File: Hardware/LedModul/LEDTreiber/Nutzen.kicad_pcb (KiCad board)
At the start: 2 copper layers, 84 x 84 mm, 400 parts, among them J1 Conn_01x01_Pin, J2 Conn_01x01_Pin, J3 Conn_01x01_Pin, J4 Conn_01x01_Pin, J5 Conn_01x01_Pin, U1 TPS92200DxRXL, U2 TVS2700DRV

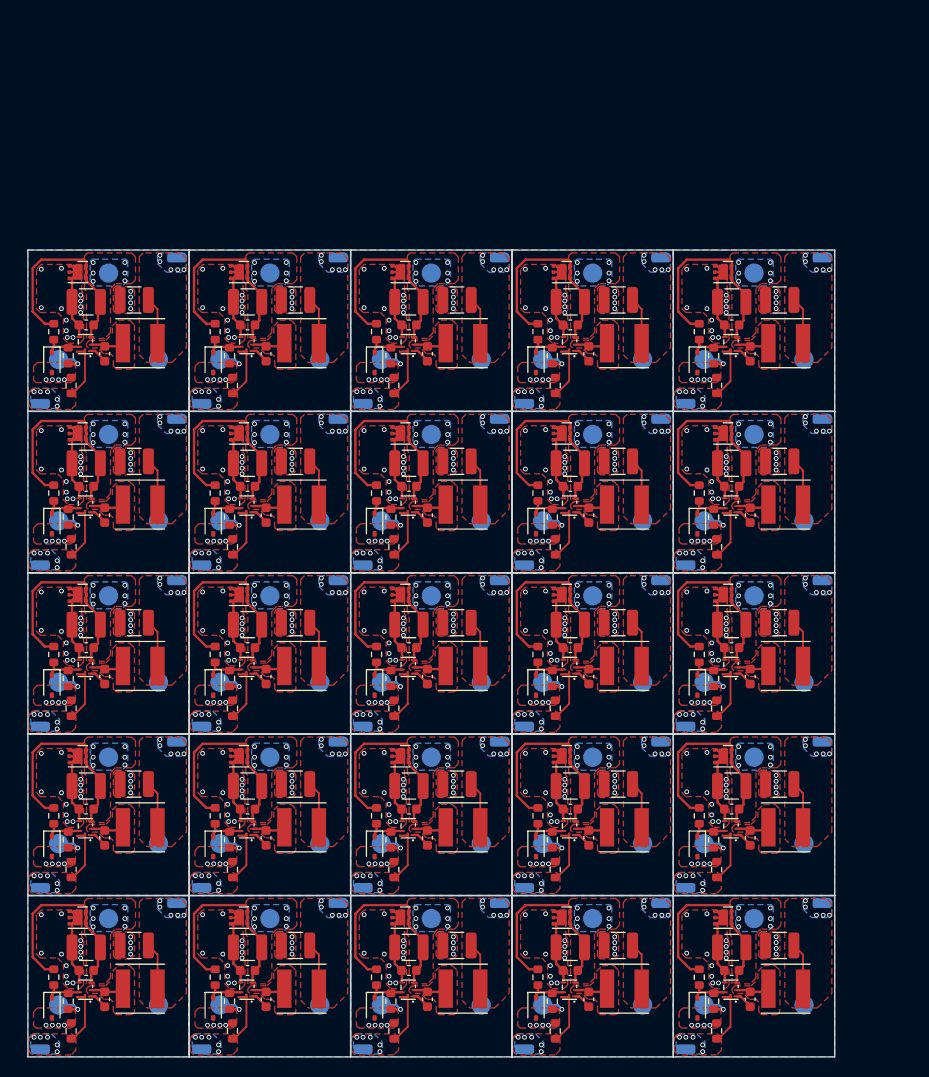
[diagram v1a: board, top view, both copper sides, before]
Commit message: added Pcb name and version to silkscreen
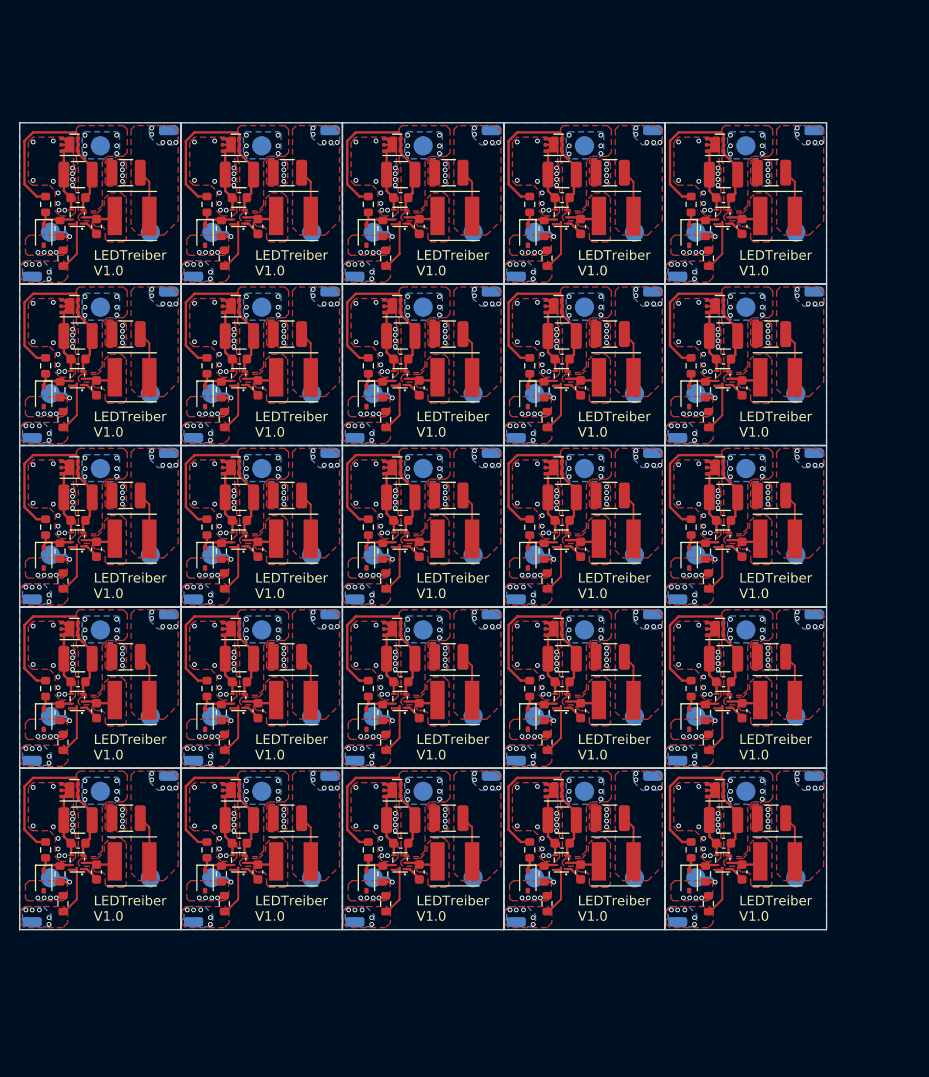
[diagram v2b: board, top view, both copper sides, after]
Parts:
- removed the C1 at (131.5, 94.8)
- removed the C1 at (131.5, 128.4)
- removed the C1 at (81.1, 94.8)
- removed the C1 at (97.9, 61.2)
- removed the C1 at (97.9, 128.4)
- removed the C1 at (81.1, 128.4)
- removed the C1 at (148.3, 94.8)
- removed the C1 at (131.5, 78.0)
- removed the C1 at (81.1, 61.2)
- removed the C1 at (114.7, 111.6)
- removed the C1 at (97.9, 78.0)
- removed the C1 at (114.7, 78.0)
- removed the C1 at (81.1, 78.0)
- removed the C1 at (131.5, 61.2)
- removed the C1 at (97.9, 111.6)
- removed the C1 at (114.7, 61.2)
- removed the C1 at (114.7, 94.8)
- removed the C1 at (97.9, 94.8)
- removed the C1 at (148.3, 111.6)
- removed the C1 at (148.3, 61.2)
- removed the C1 at (81.1, 111.6)
- removed the C1 at (148.3, 78.0)
- removed the C1 at (148.3, 128.4)
- removed the C1 at (131.5, 111.6)
- removed the C1 at (114.7, 128.4)
- removed the C2 at (128.4, 134.0)
- removed the C2 at (128.4, 66.8)
- removed the C2 at (111.6, 117.2)
- removed the C2 at (111.6, 66.8)
- removed the C2 at (128.4, 83.6)
- removed the C2 at (94.8, 100.4)
- removed the C2 at (94.8, 66.8)
- removed the C2 at (78.0, 134.0)
- removed the C2 at (145.2, 83.6)
- removed the C2 at (145.2, 66.8)
- removed the C2 at (94.8, 117.2)
- removed the C2 at (78.0, 117.2)
- removed the C2 at (78.0, 83.6)
- removed the C2 at (145.2, 134.0)
- removed the C2 at (128.4, 117.2)
- removed the C2 at (111.6, 100.4)
- removed the C2 at (111.6, 83.6)
- removed the C2 at (78.0, 100.4)
- removed the C2 at (111.6, 134.0)
- removed the C2 at (78.0, 66.8)
- removed the C2 at (94.8, 83.6)
- removed the C2 at (145.2, 100.4)
- removed the C2 at (94.8, 134.0)
- removed the C2 at (145.2, 117.2)
- removed the C2 at (128.4, 100.4)
- removed the C3 at (143.3, 111.8)
- removed the C3 at (143.3, 95.0)
- removed the C3 at (92.9, 128.6)
- removed the C3 at (92.9, 78.2)
- removed the C3 at (92.9, 95.0)
- removed the C3 at (126.5, 61.4)
- removed the C3 at (109.7, 61.4)
- removed the C3 at (143.3, 128.6)
- removed the C3 at (76.1, 95.0)
- removed the C3 at (126.5, 78.2)
- removed the C3 at (143.3, 61.4)
- removed the C3 at (109.7, 78.2)
- removed the C3 at (76.1, 78.2)
- removed the C3 at (109.7, 128.6)
- removed the C3 at (126.5, 128.6)
- removed the C3 at (76.1, 111.8)
- removed the C3 at (109.7, 95.0)
- removed the C3 at (109.7, 111.8)
- removed the C3 at (143.3, 78.2)
- removed the C3 at (126.5, 111.8)
- removed the C3 at (126.5, 95.0)
- removed the C3 at (76.1, 61.4)
- removed the C3 at (92.9, 61.4)
- removed the C3 at (76.1, 128.6)
- removed the C3 at (92.9, 111.8)
- removed the C4 at (143.3, 97.4)
- removed the C4 at (109.7, 63.8)
- removed the C4 at (143.3, 131.0)
- removed the C4 at (126.5, 97.4)
- removed the C4 at (76.1, 97.4)
- removed the C4 at (76.1, 63.8)
- removed the C4 at (109.7, 97.4)
- removed the C4 at (92.9, 63.8)
- removed the C4 at (143.3, 114.2)
- removed the C4 at (143.3, 80.6)
- removed the C4 at (109.7, 114.2)
- removed the C4 at (76.1, 80.6)
- removed the C4 at (109.7, 131.0)
- removed the C4 at (92.9, 131.0)
- removed the C4 at (143.3, 63.8)
- removed the C4 at (76.1, 114.2)
- removed the C4 at (92.9, 114.2)
- removed the C4 at (126.5, 114.2)
- removed the C4 at (109.7, 80.6)
- removed the C4 at (92.9, 80.6)
- removed the C4 at (76.1, 131.0)
- removed the C4 at (92.9, 97.4)
- removed the C4 at (126.5, 131.0)
- removed the C4 at (126.5, 80.6)
- removed the C4 at (126.5, 63.8)
- removed the D1 at (122.9, 84.5)
- removed the D1 at (89.3, 84.5)
- removed the D1 at (122.9, 134.9)
- removed the D1 at (139.7, 134.9)
- removed the D1 at (89.3, 134.9)
- removed the D1 at (89.3, 67.7)
- removed the D1 at (89.3, 101.3)
- removed the D1 at (106.1, 118.1)
- removed the D1 at (106.1, 101.3)
- removed the D1 at (72.5, 134.9)
- removed the D1 at (72.5, 84.5)
- removed the D1 at (89.3, 118.1)
- removed the D1 at (139.7, 118.1)
- removed the D1 at (139.7, 101.3)
- removed the D1 at (106.1, 67.7)
- removed the D1 at (139.7, 84.5)
- removed the D1 at (122.9, 101.3)
- removed the D1 at (72.5, 101.3)
- removed the D1 at (72.5, 67.7)
- removed the D1 at (122.9, 118.1)
- removed the D1 at (72.5, 118.1)
- removed the D1 at (122.9, 67.7)
- removed the D1 at (106.1, 134.9)
- removed the D1 at (106.1, 84.5)
- removed the D1 at (139.7, 67.7)
- removed the J1 at (135.9, 73.6)
- removed the J1 at (119.1, 124.0)
- removed the J1 at (152.7, 56.8)
- removed the J1 at (152.7, 124.0)
- removed the J1 at (102.3, 90.4)
- removed the J1 at (102.3, 73.6)
- removed the J1 at (85.5, 90.4)
- removed the J1 at (152.7, 73.6)
- removed the J1 at (135.9, 56.8)
- removed the J1 at (119.1, 90.4)
- removed the J1 at (135.9, 107.2)
- removed the J1 at (119.1, 56.8)
- removed the J1 at (152.7, 107.2)
- removed the J1 at (152.7, 90.4)
- removed the J1 at (85.5, 73.6)
- removed the J1 at (135.9, 124.0)
- removed the J1 at (85.5, 124.0)
- removed the J1 at (102.3, 56.8)
- removed the J1 at (102.3, 124.0)
- removed the J1 at (119.1, 73.6)
- removed the J1 at (119.1, 107.2)
- removed the J1 at (102.3, 107.2)
- removed the J1 at (85.5, 56.8)
- removed the J1 at (135.9, 90.4)
- removed the J1 at (85.5, 107.2)
- removed the J2 at (71.3, 122.4)
- removed the J2 at (71.3, 139.2)
- removed the J2 at (121.7, 105.6)
- removed the J2 at (104.9, 88.8)
- removed the J2 at (138.5, 88.8)
- removed the J2 at (104.9, 72.0)
- removed the J2 at (104.9, 139.2)
- removed the J2 at (138.5, 139.2)
- removed the J2 at (88.1, 88.8)
- removed the J2 at (71.3, 72.0)
- removed the J2 at (88.1, 122.4)
- removed the J2 at (104.9, 122.4)
- removed the J2 at (121.7, 88.8)
- removed the J2 at (88.1, 72.0)
- removed the J2 at (138.5, 122.4)
- removed the J2 at (138.5, 72.0)
- removed the J2 at (121.7, 122.4)
- removed the J2 at (121.7, 139.2)
- removed the J2 at (71.3, 88.8)
- removed the J2 at (121.7, 72.0)
- removed the J2 at (88.1, 139.2)
- removed the J2 at (104.9, 105.6)
- removed the J2 at (71.3, 105.6)
- removed the J2 at (88.1, 105.6)
- removed the J2 at (138.5, 105.6)
- removed the J3 at (123.6, 101.0)
- removed the J3 at (73.2, 84.2)
- removed the J3 at (73.2, 134.6)
- removed the J3 at (73.2, 67.4)
- removed the J3 at (106.8, 67.4)
- removed the J3 at (90.0, 101.0)
- removed the J3 at (123.6, 134.6)
- removed the J3 at (140.4, 101.0)
- removed the J3 at (140.4, 84.2)
- removed the J3 at (106.8, 84.2)
- removed the J3 at (123.6, 117.8)
- removed the J3 at (123.6, 67.4)
- removed the J3 at (106.8, 134.6)
- removed the J3 at (73.2, 117.8)
- removed the J3 at (90.0, 84.2)
- removed the J3 at (106.8, 101.0)
- removed the J3 at (106.8, 117.8)
- removed the J3 at (123.6, 84.2)
- removed the J3 at (90.0, 134.6)
- removed the J3 at (140.4, 67.4)
- removed the J3 at (90.0, 67.4)
- removed the J3 at (73.2, 101.0)
- removed the J3 at (90.0, 117.8)
- removed the J3 at (140.4, 117.8)
- removed the J3 at (140.4, 134.6)
- removed the J4 at (78.4, 75.2)
- removed the J4 at (145.6, 92.0)
- removed the J4 at (112.0, 92.0)
- removed the J4 at (78.4, 92.0)
- removed the J4 at (112.0, 108.8)
- removed the J4 at (128.8, 108.8)
- removed the J4 at (95.2, 92.0)
- removed the J4 at (145.6, 75.2)
- removed the J4 at (145.6, 58.4)
- removed the J4 at (95.2, 75.2)
- removed the J4 at (112.0, 75.2)
- removed the J4 at (78.4, 58.4)
- removed the J4 at (78.4, 125.6)
- removed the J4 at (128.8, 92.0)
- removed the J4 at (128.8, 125.6)
- removed the J4 at (95.2, 125.6)
- removed the J4 at (112.0, 58.4)
- removed the J4 at (78.4, 108.8)
- removed the J4 at (145.6, 108.8)
- removed the J4 at (95.2, 108.8)
- removed the J4 at (128.8, 58.4)
- removed the J4 at (145.6, 125.6)
- removed the J4 at (95.2, 58.4)
- removed the J4 at (112.0, 125.6)
- removed the J4 at (128.8, 75.2)
- removed the J5 at (83.6, 117.8)
- removed the J5 at (117.2, 134.6)
- removed the J5 at (134.0, 67.4)
- removed the J5 at (150.8, 117.8)
- removed the J5 at (100.4, 101.0)
- removed the J5 at (150.8, 134.6)
- removed the J5 at (100.4, 117.8)
- removed the J5 at (134.0, 117.8)
- removed the J5 at (117.2, 117.8)
- removed the J5 at (83.6, 101.0)
- removed the J5 at (150.8, 84.2)
- removed the J5 at (83.6, 67.4)
- removed the J5 at (134.0, 84.2)
- removed the J5 at (150.8, 67.4)
- removed the J5 at (83.6, 134.6)
- removed the J5 at (100.4, 134.6)
- removed the J5 at (100.4, 84.2)
- removed the J5 at (117.2, 84.2)
- removed the J5 at (83.6, 84.2)
- removed the J5 at (150.8, 101.0)
- removed the J5 at (117.2, 101.0)
- removed the J5 at (100.4, 67.4)
- removed the J5 at (117.2, 67.4)
- removed the J5 at (134.0, 134.6)
- removed the J5 at (134.0, 101.0)
- removed the L1 at (148.9, 82.5)
- removed the L1 at (98.5, 82.5)
- removed the L1 at (148.9, 99.3)
- removed the L1 at (115.3, 132.9)
- removed the L1 at (98.5, 116.1)
- removed the L1 at (81.7, 65.7)
- removed the L1 at (115.3, 82.5)
- removed the L1 at (81.7, 99.3)
- removed the L1 at (98.5, 65.7)
- removed the L1 at (81.7, 82.5)
- removed the L1 at (81.7, 132.9)
- removed the L1 at (115.3, 99.3)
- removed the L1 at (148.9, 65.7)
- removed the L1 at (98.5, 132.9)
- removed the L1 at (132.1, 132.9)
- removed the L1 at (98.5, 99.3)
- removed the L1 at (81.7, 116.1)
- removed the L1 at (148.9, 132.9)
- removed the L1 at (132.1, 65.7)
- removed the L1 at (115.3, 65.7)
- removed the L1 at (115.3, 116.1)
- removed the L1 at (132.1, 116.1)
- removed the L1 at (132.1, 99.3)
- removed the L1 at (148.9, 116.1)
- removed the L1 at (132.1, 82.5)
- removed the R1 at (123.1, 64.5)
- removed the R1 at (89.5, 64.5)
- removed the R1 at (123.1, 131.7)
- removed the R1 at (139.9, 98.1)
- removed the R1 at (89.5, 114.9)
- removed the R1 at (72.7, 81.3)
- removed the R1 at (106.3, 114.9)
- removed the R1 at (123.1, 98.1)
- removed the R1 at (106.3, 98.1)
- removed the R1 at (72.7, 131.7)
- removed the R1 at (139.9, 64.5)
- removed the R1 at (72.7, 64.5)
- removed the R1 at (123.1, 114.9)
- removed the R1 at (72.7, 114.9)
- removed the R1 at (89.5, 98.1)
- removed the R1 at (139.9, 81.3)
- removed the R1 at (139.9, 114.9)
- removed the R1 at (72.7, 98.1)
- removed the R1 at (106.3, 64.5)
- removed the R1 at (139.9, 131.7)
- removed the R1 at (106.3, 131.7)
- removed the R1 at (123.1, 81.3)
- removed the R1 at (89.5, 131.7)
- removed the R1 at (89.5, 81.3)
- removed the R1 at (106.3, 81.3)
- removed the R2 at (91.3, 86.9)
- removed the R2 at (141.7, 137.3)
- removed the R2 at (108.1, 103.7)
- removed the R2 at (91.3, 120.5)
- removed the R2 at (74.5, 120.5)
- removed the R2 at (91.3, 137.3)
- removed the R2 at (74.5, 137.3)
- removed the R2 at (124.9, 86.9)
- removed the R2 at (124.9, 137.3)
- removed the R2 at (108.1, 86.9)
- removed the R2 at (141.7, 103.7)
- removed the R2 at (108.1, 120.5)
- removed the R2 at (124.9, 120.5)
- removed the R2 at (124.9, 70.1)
- removed the R2 at (141.7, 70.1)
- removed the R2 at (91.3, 103.7)
- removed the R2 at (74.5, 86.9)
- removed the R2 at (108.1, 137.3)
- removed the R2 at (91.3, 70.1)
- removed the R2 at (124.9, 103.7)
- removed the R2 at (108.1, 70.1)
- removed the R2 at (141.7, 120.5)
- removed the R2 at (141.7, 86.9)
- removed the R2 at (74.5, 103.7)
- removed the R2 at (74.5, 70.1)
- removed the R3 at (124.6, 117.4)
- removed the R3 at (124.6, 67.0)
- removed the R3 at (107.8, 117.4)
- removed the R3 at (91.0, 117.4)
- removed the R3 at (74.2, 117.4)
- removed the R3 at (107.8, 100.6)
- removed the R3 at (74.2, 134.2)
- removed the R3 at (91.0, 83.8)
- removed the R3 at (91.0, 67.0)
- removed the R3 at (141.4, 83.8)
- removed the R3 at (124.6, 134.2)
- removed the R3 at (91.0, 134.2)
- removed the R3 at (141.4, 134.2)
- removed the R3 at (141.4, 100.6)
- removed the R3 at (74.2, 100.6)
- removed the R3 at (141.4, 67.0)
- removed the R3 at (124.6, 100.6)
- removed the R3 at (74.2, 83.8)
- removed the R3 at (107.8, 67.0)
- removed the R3 at (74.2, 67.0)
- removed the R3 at (124.6, 83.8)
- removed the R3 at (107.8, 83.8)
- removed the R3 at (91.0, 100.6)
- removed the R3 at (141.4, 117.4)
- removed the R3 at (107.8, 134.2)
- removed the U1 at (76.0, 133.0)
- removed the U1 at (109.6, 116.2)
- removed the U1 at (126.4, 82.6)
- removed the U1 at (92.8, 99.4)
- removed the U1 at (76.0, 82.6)
- removed the U1 at (143.2, 82.6)
- removed the U1 at (143.2, 133.0)
- removed the U1 at (126.4, 99.4)
- removed the U1 at (92.8, 65.8)
- removed the U1 at (92.8, 133.0)
- removed the U1 at (76.0, 116.2)
- removed the U1 at (109.6, 65.8)
- removed the U1 at (76.0, 65.8)
- removed the U1 at (109.6, 133.0)
- removed the U1 at (126.4, 116.2)
- removed the U1 at (126.4, 65.8)
- removed the U1 at (143.2, 116.2)
- removed the U1 at (126.4, 133.0)
- removed the U1 at (109.6, 99.4)
- removed the U1 at (143.2, 65.8)
- removed the U1 at (143.2, 99.4)
- removed the U1 at (76.0, 99.4)
- removed the U1 at (92.8, 116.2)
- removed the U1 at (109.6, 82.6)
- removed the U1 at (92.8, 82.6)
- removed the U2 at (75.2, 108.7)
- removed the U2 at (125.6, 108.7)
- removed the U2 at (125.6, 91.9)
- removed the U2 at (92.0, 125.5)
- removed the U2 at (142.4, 108.7)
- removed the U2 at (92.0, 75.1)
- removed the U2 at (75.2, 125.5)
- removed the U2 at (108.8, 108.7)
- removed the U2 at (75.2, 91.9)
- removed the U2 at (142.4, 75.1)
- removed the U2 at (108.8, 125.5)
- removed the U2 at (108.8, 91.9)
- removed the U2 at (92.0, 108.7)
- removed the U2 at (142.4, 58.3)
- removed the U2 at (108.8, 75.1)
- removed the U2 at (142.4, 91.9)
- removed the U2 at (75.2, 58.3)
- removed the U2 at (75.2, 75.1)
- removed the U2 at (125.6, 75.1)
- removed the U2 at (125.6, 58.3)
- removed the U2 at (108.8, 58.3)
- removed the U2 at (125.6, 125.5)
- removed the U2 at (92.0, 91.9)
- removed the U2 at (142.4, 125.5)
- removed the U2 at (92.0, 58.3)
- added C1: 10µ, Capacitor_SMD:C_1210_3225Metric, F.Cu at (130.6, 64.8)
- added C1: 10µ, Capacitor_SMD:C_1210_3225Metric, F.Cu at (97.0, 81.5)
- added C1: 10µ, Capacitor_SMD:C_1210_3225Metric, F.Cu at (80.2, 115.2)
- added C1: 10µ, Capacitor_SMD:C_1210_3225Metric, F.Cu at (97.0, 98.3)
- added C1: 10µ, Capacitor_SMD:C_1210_3225Metric, F.Cu at (113.8, 98.3)
- added C1: 10µ, Capacitor_SMD:C_1210_3225Metric, F.Cu at (147.4, 115.2)
- added C1: 10µ, Capacitor_SMD:C_1210_3225Metric, F.Cu at (113.8, 64.8)
- added C1: 10µ, Capacitor_SMD:C_1210_3225Metric, F.Cu at (130.6, 98.3)
- added C1: 10µ, Capacitor_SMD:C_1210_3225Metric, F.Cu at (113.8, 48.0)
- added C1: 10µ, Capacitor_SMD:C_1210_3225Metric, F.Cu at (80.2, 81.5)
- added C1: 10µ, Capacitor_SMD:C_1210_3225Metric, F.Cu at (97.0, 64.8)
- added C1: 10µ, Capacitor_SMD:C_1210_3225Metric, F.Cu at (147.4, 98.3)
- added C1: 10µ, Capacitor_SMD:C_1210_3225Metric, F.Cu at (130.6, 81.5)
- added C1: 10µ, Capacitor_SMD:C_1210_3225Metric, F.Cu at (147.4, 81.5)
- added C1: 10µ, Capacitor_SMD:C_1210_3225Metric, F.Cu at (113.8, 115.2)
- added C1: 10µ, Capacitor_SMD:C_1210_3225Metric, F.Cu at (130.6, 48.0)
- added C1: 10µ, Capacitor_SMD:C_1210_3225Metric, F.Cu at (147.4, 64.8)
- added C1: 10µ, Capacitor_SMD:C_1210_3225Metric, F.Cu at (147.4, 48.0)
- added C1: 10µ, Capacitor_SMD:C_1210_3225Metric, F.Cu at (80.2, 98.3)
- added C1: 10µ, Capacitor_SMD:C_1210_3225Metric, F.Cu at (97.0, 48.0)
- added C1: 10µ, Capacitor_SMD:C_1210_3225Metric, F.Cu at (130.6, 115.2)
- added C1: 10µ, Capacitor_SMD:C_1210_3225Metric, F.Cu at (80.2, 64.8)
- added C1: 10µ, Capacitor_SMD:C_1210_3225Metric, F.Cu at (97.0, 115.2)
- added C1: 10µ, Capacitor_SMD:C_1210_3225Metric, F.Cu at (113.8, 81.5)
- added C1: 10µ, Capacitor_SMD:C_1210_3225Metric, F.Cu at (80.2, 48.0)
- added C2: 100n, Capacitor_SMD:C_0603_1608Metric, F.Cu at (110.8, 53.5)
- added C2: 100n, Capacitor_SMD:C_0603_1608Metric, F.Cu at (110.8, 120.8)
- added C2: 100n, Capacitor_SMD:C_0603_1608Metric, F.Cu at (127.5, 53.5)
- added C2: 100n, Capacitor_SMD:C_0603_1608Metric, F.Cu at (110.8, 87.2)
- added C2: 100n, Capacitor_SMD:C_0603_1608Metric, F.Cu at (110.8, 70.3)
- added C2: 100n, Capacitor_SMD:C_0603_1608Metric, F.Cu at (144.3, 53.5)
- added C2: 100n, Capacitor_SMD:C_0603_1608Metric, F.Cu at (94.0, 120.8)
- added C2: 100n, Capacitor_SMD:C_0603_1608Metric, F.Cu at (77.2, 87.2)
- added C2: 100n, Capacitor_SMD:C_0603_1608Metric, F.Cu at (77.2, 70.3)
- added C2: 100n, Capacitor_SMD:C_0603_1608Metric, F.Cu at (127.5, 104.0)
- added C2: 100n, Capacitor_SMD:C_0603_1608Metric, F.Cu at (144.3, 87.2)
- added C2: 100n, Capacitor_SMD:C_0603_1608Metric, F.Cu at (77.2, 53.5)
- added C2: 100n, Capacitor_SMD:C_0603_1608Metric, F.Cu at (94.0, 53.5)
- added C2: 100n, Capacitor_SMD:C_0603_1608Metric, F.Cu at (94.0, 104.0)
- added C2: 100n, Capacitor_SMD:C_0603_1608Metric, F.Cu at (144.3, 104.0)
- added C2: 100n, Capacitor_SMD:C_0603_1608Metric, F.Cu at (77.2, 104.0)
- added C2: 100n, Capacitor_SMD:C_0603_1608Metric, F.Cu at (127.5, 87.2)
- added C2: 100n, Capacitor_SMD:C_0603_1608Metric, F.Cu at (110.8, 104.0)
- added C2: 100n, Capacitor_SMD:C_0603_1608Metric, F.Cu at (144.3, 120.8)
- added C2: 100n, Capacitor_SMD:C_0603_1608Metric, F.Cu at (144.3, 70.3)
- added C2: 100n, Capacitor_SMD:C_0603_1608Metric, F.Cu at (94.0, 87.2)
- added C2: 100n, Capacitor_SMD:C_0603_1608Metric, F.Cu at (127.5, 70.3)
- added C2: 100n, Capacitor_SMD:C_0603_1608Metric, F.Cu at (127.5, 120.8)
- added C2: 100n, Capacitor_SMD:C_0603_1608Metric, F.Cu at (77.2, 120.8)
- added C2: 100n, Capacitor_SMD:C_0603_1608Metric, F.Cu at (94.0, 70.3)
- added C3: 10µ, Capacitor_SMD:C_1210_3225Metric, F.Cu at (75.2, 115.3)
- added C3: 10µ, Capacitor_SMD:C_1210_3225Metric, F.Cu at (142.4, 65.0)
- added C3: 10µ, Capacitor_SMD:C_1210_3225Metric, F.Cu at (142.4, 81.8)
- added C3: 10µ, Capacitor_SMD:C_1210_3225Metric, F.Cu at (75.2, 98.5)
- added C3: 10µ, Capacitor_SMD:C_1210_3225Metric, F.Cu at (125.6, 98.5)
- added C3: 10µ, Capacitor_SMD:C_1210_3225Metric, F.Cu at (108.8, 115.3)
- added C3: 10µ, Capacitor_SMD:C_1210_3225Metric, F.Cu at (142.4, 98.5)
- added C3: 10µ, Capacitor_SMD:C_1210_3225Metric, F.Cu at (75.2, 81.8)
- added C3: 10µ, Capacitor_SMD:C_1210_3225Metric, F.Cu at (92.0, 98.5)
- added C3: 10µ, Capacitor_SMD:C_1210_3225Metric, F.Cu at (125.6, 48.1)
- added C3: 10µ, Capacitor_SMD:C_1210_3225Metric, F.Cu at (108.8, 65.0)
- added C3: 10µ, Capacitor_SMD:C_1210_3225Metric, F.Cu at (142.4, 48.1)
- added C3: 10µ, Capacitor_SMD:C_1210_3225Metric, F.Cu at (108.8, 81.8)
- added C3: 10µ, Capacitor_SMD:C_1210_3225Metric, F.Cu at (92.0, 81.8)
- added C3: 10µ, Capacitor_SMD:C_1210_3225Metric, F.Cu at (108.8, 48.1)
- added C3: 10µ, Capacitor_SMD:C_1210_3225Metric, F.Cu at (125.6, 65.0)
- added C3: 10µ, Capacitor_SMD:C_1210_3225Metric, F.Cu at (75.2, 48.1)
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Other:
- board text added: "LEDTreiber V1.0"

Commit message: V1.1
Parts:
- removed the C1 at (130.6, 64.8)
- removed the C1 at (97.0, 81.5)
- removed the C1 at (80.2, 115.2)
- removed the C1 at (97.0, 98.3)
- removed the C1 at (113.8, 98.3)
- removed the C1 at (147.4, 115.2)
- removed the C1 at (113.8, 64.8)
- removed the C1 at (130.6, 98.3)
- removed the C1 at (113.8, 48.0)
- removed the C1 at (80.2, 81.5)
- removed the C1 at (97.0, 64.8)
- removed the C1 at (147.4, 98.3)
- removed the C1 at (130.6, 81.5)
- removed the C1 at (147.4, 81.5)
- removed the C1 at (113.8, 115.2)
- removed the C1 at (130.6, 48.0)
- removed the C1 at (147.4, 64.8)
- removed the C1 at (147.4, 48.0)
- removed the C1 at (80.2, 98.3)
- removed the C1 at (97.0, 48.0)
- removed the C1 at (130.6, 115.2)
- removed the C1 at (80.2, 64.8)
- removed the C1 at (97.0, 115.2)
- removed the C1 at (113.8, 81.5)
- removed the C1 at (80.2, 48.0)
- removed the C2 at (110.8, 53.5)
- removed the C2 at (110.8, 120.8)
- removed the C2 at (127.5, 53.5)
- removed the C2 at (110.8, 87.2)
- removed the C2 at (110.8, 70.3)
- removed the C2 at (144.3, 53.5)
- removed the C2 at (94.0, 120.8)
- removed the C2 at (77.2, 87.2)
- removed the C2 at (77.2, 70.3)
- removed the C2 at (127.5, 104.0)
- removed the C2 at (144.3, 87.2)
- removed the C2 at (77.2, 53.5)
- removed the C2 at (94.0, 53.5)
- removed the C2 at (94.0, 104.0)
- removed the C2 at (144.3, 104.0)
- removed the C2 at (77.2, 104.0)
- removed the C2 at (127.5, 87.2)
- removed the C2 at (110.8, 104.0)
- removed the C2 at (144.3, 120.8)
- removed the C2 at (144.3, 70.3)
- removed the C2 at (94.0, 87.2)
- removed the C2 at (127.5, 70.3)
- removed the C2 at (127.5, 120.8)
- removed the C2 at (77.2, 120.8)
- removed the C2 at (94.0, 70.3)
- removed the C3 at (75.2, 115.3)
- removed the C3 at (142.4, 65.0)
- removed the C3 at (142.4, 81.8)
- removed the C3 at (75.2, 98.5)
- removed the C3 at (125.6, 98.5)
- removed the C3 at (108.8, 115.3)
- removed the C3 at (142.4, 98.5)
- removed the C3 at (75.2, 81.8)
- removed the C3 at (92.0, 98.5)
- removed the C3 at (125.6, 48.1)
- removed the C3 at (108.8, 65.0)
- removed the C3 at (142.4, 48.1)
- removed the C3 at (108.8, 81.8)
- removed the C3 at (92.0, 81.8)
- removed the C3 at (108.8, 48.1)
- removed the C3 at (125.6, 65.0)
- removed the C3 at (75.2, 48.1)
- removed the C3 at (92.0, 48.1)
- removed the C3 at (142.4, 115.3)
- removed the C3 at (125.6, 81.8)
- removed the C3 at (75.2, 65.0)
- removed the C3 at (125.6, 115.3)
- removed the C3 at (108.8, 98.5)
- removed the C3 at (92.0, 65.0)
- removed the C3 at (92.0, 115.3)
- removed the C4 at (92.0, 117.8)
- removed the C4 at (125.6, 67.3)
- removed the C4 at (142.4, 50.5)
- removed the C4 at (125.6, 101.0)
- removed the C4 at (142.4, 101.0)
- removed the C4 at (125.6, 50.5)
- removed the C4 at (108.8, 50.5)
- removed the C4 at (108.8, 84.2)
- removed the C4 at (75.2, 101.0)
- removed the C4 at (142.4, 84.2)
- removed the C4 at (142.4, 117.8)
- removed the C4 at (108.8, 67.3)
- removed the C4 at (92.0, 84.2)
- removed the C4 at (92.0, 67.3)
- removed the C4 at (75.2, 117.8)
- removed the C4 at (92.0, 101.0)
- removed the C4 at (125.6, 84.2)
- removed the C4 at (75.2, 67.3)
- removed the C4 at (75.2, 84.2)
- removed the C4 at (142.4, 67.3)
- removed the C4 at (75.2, 50.5)
- removed the C4 at (108.8, 117.8)
- removed the C4 at (108.8, 101.0)
- removed the C4 at (125.6, 117.8)
- removed the C4 at (92.0, 50.5)
- removed the D1 at (88.5, 88.0)
- removed the D1 at (71.7, 54.5)
- removed the D1 at (88.5, 71.2)
- removed the D1 at (71.7, 71.2)
- removed the D1 at (71.7, 104.8)
- removed the D1 at (88.5, 104.8)
- removed the D1 at (88.5, 54.5)
- removed the D1 at (138.8, 71.2)
- removed the D1 at (122.0, 88.0)
- removed the D1 at (88.5, 121.7)
- removed the D1 at (105.2, 121.7)
- removed the D1 at (122.0, 104.8)
- removed the D1 at (138.8, 121.7)
- removed the D1 at (71.7, 88.0)
- removed the D1 at (105.2, 71.2)
- removed the D1 at (105.2, 54.5)
- removed the D1 at (138.8, 54.5)
- removed the D1 at (122.0, 121.7)
- removed the D1 at (105.2, 88.0)
- removed the D1 at (138.8, 104.8)
- removed the D1 at (105.2, 104.8)
- removed the D1 at (122.0, 71.2)
- removed the D1 at (138.8, 88.0)
- removed the D1 at (71.7, 121.7)
- removed the D1 at (122.0, 54.5)
- removed the J1 at (118.2, 43.5)
- removed the J1 at (118.2, 110.8)
- removed the J1 at (101.5, 94.0)
- removed the J1 at (151.8, 110.8)
- removed the J1 at (84.7, 110.8)
- removed the J1 at (118.2, 60.4)
- removed the J1 at (151.8, 77.2)
- removed the J1 at (101.5, 110.8)
- removed the J1 at (135.1, 77.2)
- removed the J1 at (101.5, 60.4)
- removed the J1 at (84.7, 94.0)
- removed the J1 at (118.2, 94.0)
- removed the J1 at (151.8, 60.4)
- removed the J1 at (118.2, 77.2)
- removed the J1 at (151.8, 43.5)
- removed the J1 at (84.7, 77.2)
- removed the J1 at (101.5, 43.5)
- removed the J1 at (151.8, 94.0)
- removed the J1 at (135.1, 94.0)
- removed the J1 at (84.7, 60.4)
- removed the J1 at (135.1, 43.5)
- removed the J1 at (135.1, 110.8)
- removed the J1 at (84.7, 43.5)
- removed the J1 at (135.1, 60.4)
- removed the J1 at (101.5, 77.2)
- removed the J2 at (104.0, 58.8)
- removed the J2 at (70.5, 75.5)
- removed the J2 at (87.2, 92.3)
- removed the J2 at (104.0, 92.3)
- removed the J2 at (137.7, 126.0)
- removed the J2 at (70.5, 126.0)
- removed the J2 at (120.8, 58.8)
- removed the J2 at (104.0, 75.5)
- removed the J2 at (120.8, 75.5)
- removed the J2 at (120.8, 126.0)
- removed the J2 at (87.2, 109.2)
- removed the J2 at (137.7, 75.5)
- removed the J2 at (70.5, 58.8)
- removed the J2 at (70.5, 92.3)
- removed the J2 at (137.7, 109.2)
- removed the J2 at (120.8, 92.3)
- removed the J2 at (120.8, 109.2)
- removed the J2 at (104.0, 126.0)
- removed the J2 at (104.0, 109.2)
- removed the J2 at (87.2, 58.8)
- removed the J2 at (137.7, 58.8)
- removed the J2 at (87.2, 126.0)
- removed the J2 at (137.7, 92.3)
- removed the J2 at (87.2, 75.5)
- removed the J2 at (70.5, 109.2)
- removed the J3 at (72.3, 71.0)
- removed the J3 at (72.3, 87.8)
- removed the J3 at (89.2, 104.5)
- removed the J3 at (139.6, 54.1)
- removed the J3 at (106.0, 104.5)
- removed the J3 at (72.3, 121.3)
- removed the J3 at (106.0, 54.1)
- removed the J3 at (106.0, 121.3)
- removed the J3 at (89.2, 54.1)
- removed the J3 at (106.0, 71.0)
- removed the J3 at (89.2, 87.8)
- removed the J3 at (122.8, 104.5)
- removed the J3 at (72.3, 104.5)
- removed the J3 at (72.3, 54.1)
- removed the J3 at (139.6, 104.5)
- removed the J3 at (89.2, 121.3)
- removed the J3 at (122.8, 121.3)
- removed the J3 at (139.6, 121.3)
- removed the J3 at (122.8, 54.1)
- removed the J3 at (89.2, 71.0)
- removed the J3 at (122.8, 71.0)
- removed the J3 at (139.6, 71.0)
- removed the J3 at (139.6, 87.8)
- removed the J3 at (122.8, 87.8)
- removed the J3 at (106.0, 87.8)
- removed the J4 at (94.3, 78.8)
- removed the J4 at (144.8, 62.0)
- removed the J4 at (77.5, 95.5)
- removed the J4 at (128.0, 45.1)
- removed the J4 at (77.5, 112.3)
- removed the J4 at (77.5, 62.0)
- removed the J4 at (111.2, 62.0)
- removed the J4 at (111.2, 45.1)
- removed the J4 at (94.3, 45.1)
- removed the J4 at (128.0, 62.0)
- removed the J4 at (144.8, 95.5)
- removed the J4 at (111.2, 95.5)
- removed the J4 at (94.3, 112.3)
- removed the J4 at (94.3, 95.5)
- removed the J4 at (77.5, 78.8)
- removed the J4 at (94.3, 62.0)
- removed the J4 at (111.2, 112.3)
- removed the J4 at (128.0, 78.8)
- removed the J4 at (128.0, 95.5)
- removed the J4 at (144.8, 45.1)
- removed the J4 at (144.8, 112.3)
- removed the J4 at (128.0, 112.3)
- removed the J4 at (144.8, 78.8)
- removed the J4 at (77.5, 45.1)
- removed the J4 at (111.2, 78.8)
- removed the J5 at (82.8, 104.5)
- removed the J5 at (82.8, 54.1)
- removed the J5 at (99.5, 87.8)
- removed the J5 at (82.8, 71.0)
- removed the J5 at (116.3, 54.1)
- removed the J5 at (149.9, 71.0)
- removed the J5 at (99.5, 121.3)
- removed the J5 at (133.2, 54.1)
- removed the J5 at (82.8, 87.8)
- removed the J5 at (149.9, 121.3)
- removed the J5 at (133.2, 71.0)
- removed the J5 at (99.5, 104.5)
- removed the J5 at (133.2, 104.5)
- removed the J5 at (116.3, 104.5)
- removed the J5 at (116.3, 87.8)
- removed the J5 at (149.9, 54.1)
- removed the J5 at (99.5, 54.1)
- removed the J5 at (149.9, 87.8)
- removed the J5 at (116.3, 121.3)
- removed the J5 at (116.3, 71.0)
- removed the J5 at (99.5, 71.0)
- removed the J5 at (82.8, 121.3)
- removed the J5 at (133.2, 87.8)
- removed the J5 at (133.2, 121.3)
- removed the J5 at (149.9, 104.5)
- removed the L1 at (131.2, 86.0)
- removed the L1 at (97.7, 52.5)
- removed the L1 at (148.1, 102.8)
- removed the L1 at (80.8, 86.0)
- removed the L1 at (114.5, 86.0)
- removed the L1 at (80.8, 102.8)
- removed the L1 at (97.7, 119.7)
- removed the L1 at (148.1, 119.7)
- removed the L1 at (114.5, 69.2)
- removed the L1 at (97.7, 86.0)
- removed the L1 at (97.7, 102.8)
- removed the L1 at (114.5, 102.8)
- removed the L1 at (131.2, 69.2)
- removed the L1 at (131.2, 52.5)
- removed the L1 at (131.2, 119.7)
- removed the L1 at (148.1, 69.2)
- removed the L1 at (148.1, 52.5)
- removed the L1 at (80.8, 119.7)
- removed the L1 at (97.7, 69.2)
- removed the L1 at (114.5, 119.7)
- removed the L1 at (148.1, 86.0)
- removed the L1 at (131.2, 102.8)
- removed the L1 at (80.8, 52.5)
- removed the L1 at (114.5, 52.5)
- removed the L1 at (80.8, 69.2)
- removed the R1 at (139.1, 118.5)
- removed the R1 at (139.1, 101.7)
- removed the R1 at (88.7, 84.8)
- removed the R1 at (122.2, 51.2)
- removed the R1 at (122.2, 68.0)
- removed the R1 at (139.1, 84.8)
- removed the R1 at (71.8, 51.2)
- removed the R1 at (71.8, 118.5)
- removed the R1 at (105.5, 84.8)
- removed the R1 at (105.5, 51.2)
- removed the R1 at (139.1, 68.0)
- removed the R1 at (139.1, 51.2)
- removed the R1 at (71.8, 84.8)
- removed the R1 at (122.2, 101.7)
- removed the R1 at (122.2, 84.8)
- removed the R1 at (88.7, 51.2)
- removed the R1 at (105.5, 68.0)
- removed the R1 at (105.5, 118.5)
- removed the R1 at (88.7, 101.7)
- removed the R1 at (71.8, 101.7)
- removed the R1 at (71.8, 68.0)
- removed the R1 at (122.2, 118.5)
- removed the R1 at (88.7, 118.5)
- removed the R1 at (105.5, 101.7)
- removed the R1 at (88.7, 68.0)
- removed the R2 at (140.8, 90.5)
- removed the R2 at (73.7, 107.2)
- removed the R2 at (140.8, 107.2)
- removed the R2 at (107.2, 107.2)
- removed the R2 at (107.2, 90.5)
- removed the R2 at (107.2, 124.0)
- removed the R2 at (90.5, 73.7)
- removed the R2 at (73.7, 73.7)
- removed the R2 at (140.8, 124.0)
- removed the R2 at (90.5, 124.0)
- removed the R2 at (90.5, 56.9)
- removed the R2 at (107.2, 73.7)
- removed the R2 at (73.7, 124.0)
- removed the R2 at (90.5, 107.2)
- removed the R2 at (140.8, 73.7)
- removed the R2 at (73.7, 56.9)
- removed the R2 at (90.5, 90.5)
- removed the R2 at (73.7, 90.5)
- removed the R2 at (124.0, 56.9)
- removed the R2 at (140.8, 56.9)
- removed the R2 at (124.0, 107.2)
- removed the R2 at (124.0, 73.7)
- removed the R2 at (107.2, 56.9)
- removed the R2 at (124.0, 90.5)
- removed the R2 at (124.0, 124.0)
- removed the R3 at (107.0, 70.5)
- removed the R3 at (73.3, 121.0)
- removed the R3 at (73.3, 53.8)
- removed the R3 at (140.6, 121.0)
- removed the R3 at (90.2, 70.5)
- removed the R3 at (90.2, 104.2)
- removed the R3 at (123.8, 70.5)
- removed the R3 at (140.6, 104.2)
- removed the R3 at (140.6, 70.5)
- removed the R3 at (123.8, 104.2)
- removed the R3 at (123.8, 87.3)
- removed the R3 at (140.6, 53.8)
- removed the R3 at (90.2, 53.8)
- removed the R3 at (123.8, 53.8)
- removed the R3 at (107.0, 87.3)
- removed the R3 at (73.3, 104.2)
- removed the R3 at (107.0, 104.2)
- removed the R3 at (73.3, 70.5)
- removed the R3 at (107.0, 121.0)
- removed the R3 at (90.2, 87.3)
- removed the R3 at (123.8, 121.0)
- removed the R3 at (90.2, 121.0)
- removed the R3 at (140.6, 87.3)
- removed the R3 at (73.3, 87.3)
- removed the R3 at (107.0, 53.8)
- removed the U1 at (108.8, 69.3)
- removed the U1 at (125.5, 52.5)
- removed the U1 at (108.8, 103.0)
- removed the U1 at (142.3, 103.0)
- removed the U1 at (125.5, 86.2)
- removed the U1 at (142.3, 69.3)
- removed the U1 at (75.2, 86.2)
- removed the U1 at (92.0, 103.0)
- removed the U1 at (92.0, 52.5)
- removed the U1 at (92.0, 119.8)
- removed the U1 at (142.3, 52.5)
- removed the U1 at (75.2, 119.8)
- removed the U1 at (142.3, 86.2)
- removed the U1 at (75.2, 52.5)
- removed the U1 at (142.3, 119.8)
- removed the U1 at (75.2, 69.3)
- removed the U1 at (125.5, 119.8)
- removed the U1 at (108.8, 119.8)
- removed the U1 at (75.2, 103.0)
- removed the U1 at (92.0, 69.3)
- removed the U1 at (108.8, 86.2)
- removed the U1 at (125.5, 103.0)
- removed the U1 at (125.5, 69.3)
- removed the U1 at (92.0, 86.2)
- removed the U1 at (108.8, 52.5)
- removed the U2 at (91.2, 61.9)
- removed the U2 at (108.0, 112.2)
- removed the U2 at (91.2, 112.2)
- removed the U2 at (141.6, 112.2)
- removed the U2 at (141.6, 45.0)
- removed the U2 at (141.6, 95.5)
- removed the U2 at (124.8, 61.9)
- removed the U2 at (141.6, 78.7)
- removed the U2 at (141.6, 61.9)
- removed the U2 at (124.8, 45.0)
- removed the U2 at (108.0, 45.0)
- removed the U2 at (91.2, 95.5)
- removed the U2 at (124.8, 95.5)
- removed the U2 at (108.0, 78.7)
- removed the U2 at (91.2, 78.7)
- removed the U2 at (74.3, 61.9)
- removed the U2 at (124.8, 78.7)
- removed the U2 at (91.2, 45.0)
- removed the U2 at (108.0, 61.9)
- removed the U2 at (74.3, 78.7)
- removed the U2 at (108.0, 95.5)
- removed the U2 at (74.3, 45.0)
- removed the U2 at (124.8, 112.2)
- removed the U2 at (74.3, 95.5)
- removed the U2 at (74.3, 112.2)
- added C1: 10µ, Capacitor_SMD:C_1210_3225Metric, F.Cu at (155.4, 54.2)
- added C1: 10µ, Capacitor_SMD:C_1210_3225Metric, F.Cu at (121.8, 87.8)
- added C1: 10µ, Capacitor_SMD:C_1210_3225Metric, F.Cu at (105.0, 87.8)
- added C1: 10µ, Capacitor_SMD:C_1210_3225Metric, F.Cu at (138.6, 87.8)
- added C1: 10µ, Capacitor_SMD:C_1210_3225Metric, F.Cu at (88.2, 71.0)
- added C1: 10µ, Capacitor_SMD:C_1210_3225Metric, F.Cu at (121.8, 104.6)
- added C1: 10µ, Capacitor_SMD:C_1210_3225Metric, F.Cu at (155.4, 37.4)
- added C1: 10µ, Capacitor_SMD:C_1210_3225Metric, F.Cu at (138.6, 104.6)
- added C1: 10µ, Capacitor_SMD:C_1210_3225Metric, F.Cu at (121.8, 71.0)
- added C1: 10µ, Capacitor_SMD:C_1210_3225Metric, F.Cu at (105.0, 104.6)
- added C1: 10µ, Capacitor_SMD:C_1210_3225Metric, F.Cu at (155.4, 104.6)
- added C1: 10µ, Capacitor_SMD:C_1210_3225Metric, F.Cu at (105.0, 71.0)
- added C1: 10µ, Capacitor_SMD:C_1210_3225Metric, F.Cu at (105.0, 54.2)
- added C1: 10µ, Capacitor_SMD:C_1210_3225Metric, F.Cu at (88.2, 87.8)
- added C1: 10µ, Capacitor_SMD:C_1210_3225Metric, F.Cu at (88.2, 37.4)
- added C1: 10µ, Capacitor_SMD:C_1210_3225Metric, F.Cu at (155.4, 87.8)
- added C1: 10µ, Capacitor_SMD:C_1210_3225Metric, F.Cu at (88.2, 104.6)
- added C1: 10µ, Capacitor_SMD:C_1210_3225Metric, F.Cu at (155.4, 71.0)
- added C1: 10µ, Capacitor_SMD:C_1210_3225Metric, F.Cu at (138.6, 37.4)
- added C1: 10µ, Capacitor_SMD:C_1210_3225Metric, F.Cu at (138.6, 71.0)
- added C1: 10µ, Capacitor_SMD:C_1210_3225Metric, F.Cu at (105.0, 37.4)
- added C1: 10µ, Capacitor_SMD:C_1210_3225Metric, F.Cu at (121.8, 54.2)
- added C1: 10µ, Capacitor_SMD:C_1210_3225Metric, F.Cu at (138.6, 54.2)
- added C1: 10µ, Capacitor_SMD:C_1210_3225Metric, F.Cu at (88.2, 54.2)
- added C1: 10µ, Capacitor_SMD:C_1210_3225Metric, F.Cu at (121.8, 37.4)
- added C2: 100n, Capacitor_SMD:C_0603_1608Metric, F.Cu at (152.3, 93.4)
- added C2: 100n, Capacitor_SMD:C_0603_1608Metric, F.Cu at (101.9, 76.6)
- added C2: 100n, Capacitor_SMD:C_0603_1608Metric, F.Cu at (101.9, 110.2)
- added C2: 100n, Capacitor_SMD:C_0603_1608Metric, F.Cu at (101.9, 59.8)
- added C2: 100n, Capacitor_SMD:C_0603_1608Metric, F.Cu at (101.9, 93.4)
- added C2: 100n, Capacitor_SMD:C_0603_1608Metric, F.Cu at (135.5, 93.4)
- added C2: 100n, Capacitor_SMD:C_0603_1608Metric, F.Cu at (85.1, 93.4)
- added C2: 100n, Capacitor_SMD:C_0603_1608Metric, F.Cu at (152.3, 59.8)
- added C2: 100n, Capacitor_SMD:C_0603_1608Metric, F.Cu at (85.1, 76.6)
- added C2: 100n, Capacitor_SMD:C_0603_1608Metric, F.Cu at (85.1, 59.8)
- added C2: 100n, Capacitor_SMD:C_0603_1608Metric, F.Cu at (101.9, 43.0)
- added C2: 100n, Capacitor_SMD:C_0603_1608Metric, F.Cu at (118.7, 93.4)
- added C2: 100n, Capacitor_SMD:C_0603_1608Metric, F.Cu at (118.7, 110.2)
- added C2: 100n, Capacitor_SMD:C_0603_1608Metric, F.Cu at (135.5, 59.8)
- added C2: 100n, Capacitor_SMD:C_0603_1608Metric, F.Cu at (135.5, 110.2)
- added C2: 100n, Capacitor_SMD:C_0603_1608Metric, F.Cu at (118.7, 76.6)
- added C2: 100n, Capacitor_SMD:C_0603_1608Metric, F.Cu at (118.7, 43.0)
- added C2: 100n, Capacitor_SMD:C_0603_1608Metric, F.Cu at (135.5, 43.0)
- added C2: 100n, Capacitor_SMD:C_0603_1608Metric, F.Cu at (152.3, 110.2)
- added C2: 100n, Capacitor_SMD:C_0603_1608Metric, F.Cu at (152.3, 43.0)
- added C2: 100n, Capacitor_SMD:C_0603_1608Metric, F.Cu at (85.1, 110.2)
- added C2: 100n, Capacitor_SMD:C_0603_1608Metric, F.Cu at (85.1, 43.0)
- added C2: 100n, Capacitor_SMD:C_0603_1608Metric, F.Cu at (118.7, 59.8)
- added C2: 100n, Capacitor_SMD:C_0603_1608Metric, F.Cu at (152.3, 76.6)
- added C2: 100n, Capacitor_SMD:C_0603_1608Metric, F.Cu at (135.5, 76.6)
- added C3: 10µ, Capacitor_SMD:C_1210_3225Metric, F.Cu at (133.6, 54.4)
- added C3: 10µ, Capacitor_SMD:C_1210_3225Metric, F.Cu at (116.8, 71.2)
- added C3: 10µ, Capacitor_SMD:C_1210_3225Metric, F.Cu at (83.2, 71.2)
- added C3: 10µ, Capacitor_SMD:C_1210_3225Metric, F.Cu at (150.4, 88.0)
- added C3: 10µ, Capacitor_SMD:C_1210_3225Metric, F.Cu at (116.8, 54.4)
- added C3: 10µ, Capacitor_SMD:C_1210_3225Metric, F.Cu at (150.4, 37.6)
- added C3: 10µ, Capacitor_SMD:C_1210_3225Metric, F.Cu at (83.2, 37.6)
- added C3: 10µ, Capacitor_SMD:C_1210_3225Metric, F.Cu at (150.4, 71.2)
- added C3: 10µ, Capacitor_SMD:C_1210_3225Metric, F.Cu at (100.0, 37.6)
- added C3: 10µ, Capacitor_SMD:C_1210_3225Metric, F.Cu at (133.6, 71.2)
- added C3: 10µ, Capacitor_SMD:C_1210_3225Metric, F.Cu at (83.2, 88.0)
- added C3: 10µ, Capacitor_SMD:C_1210_3225Metric, F.Cu at (100.0, 104.8)
- added C3: 10µ, Capacitor_SMD:C_1210_3225Metric, F.Cu at (133.6, 88.0)
- added C3: 10µ, Capacitor_SMD:C_1210_3225Metric, F.Cu at (133.6, 104.8)
- added C3: 10µ, Capacitor_SMD:C_1210_3225Metric, F.Cu at (100.0, 54.4)
- added C3: 10µ, Capacitor_SMD:C_1210_3225Metric, F.Cu at (100.0, 88.0)
- added C3: 10µ, Capacitor_SMD:C_1210_3225Metric, F.Cu at (116.8, 104.8)
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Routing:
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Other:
- board text added: "LEDTreiber V1.1"
- board text removed: "LEDTreiber V1.0"
